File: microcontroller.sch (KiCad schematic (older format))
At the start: 22 parts, among them J7 I2C, SW1 SW_Push, U2 LM1117-5.0, U3 Teensy3.2

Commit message: Add ESP-32S symbol and footprint, start integration
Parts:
- removed C6, C7: 100nF tantal, Capacitor_SMD:C_0805_2012Metric_Pad1.15x1.40mm_HandSolder, symbol Device:C
- removed D7: 1N5817, Diode_SMD:D_SMA, symbol Device:D
- removed U2: LM1117-5.0, Package_TO_SOT_SMD:SOT-223-3_TabPin2, symbol Regulator_Linear:LM1117-5.0
- added U?: ESP32-DEVKITC-32D, MODULE_ESP32-DEVKITC-32D, symbol ESP32-DEVKITC-32D:ESP32-DEVKITC-32D
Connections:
- net labels removed: VUSB
- wire segments 69 -> 55
- no-connect marks 32 -> 45
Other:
- note added: "5...15 V DC"
- note added: "Bidirectional\nBreakdown Voltage: 15.2-16.8 V"
- note added: "Default I2C: SDA: GPIO 21, SCL: GPIO 22"
- note added: "ESP32 Pin Info:\nGPIO 6-11: Do not use! (onboard SPI Flash)\nGPIO 34,35: Input only\n"
- note added: "Ioutmax=1 A (AMS1117-3.3)"
- note added: "Serial0 (USB)"
- note added: "Serial2 (WT32i)"
- note added: "Vin=4.3...15 V"
- note added: "external 5k pullup"
- note added: "onboard LED"
- note removed: "6...20 V DC"
- note removed: "Ioutmax=250 mA"
- note removed: "Serial3"
- note removed: "This Diode should be solderd to protect the USB\nport when external voltage is present. To make it \nwork, a trace on the teensy must be cut."
- moved on the sheet: D6, U3

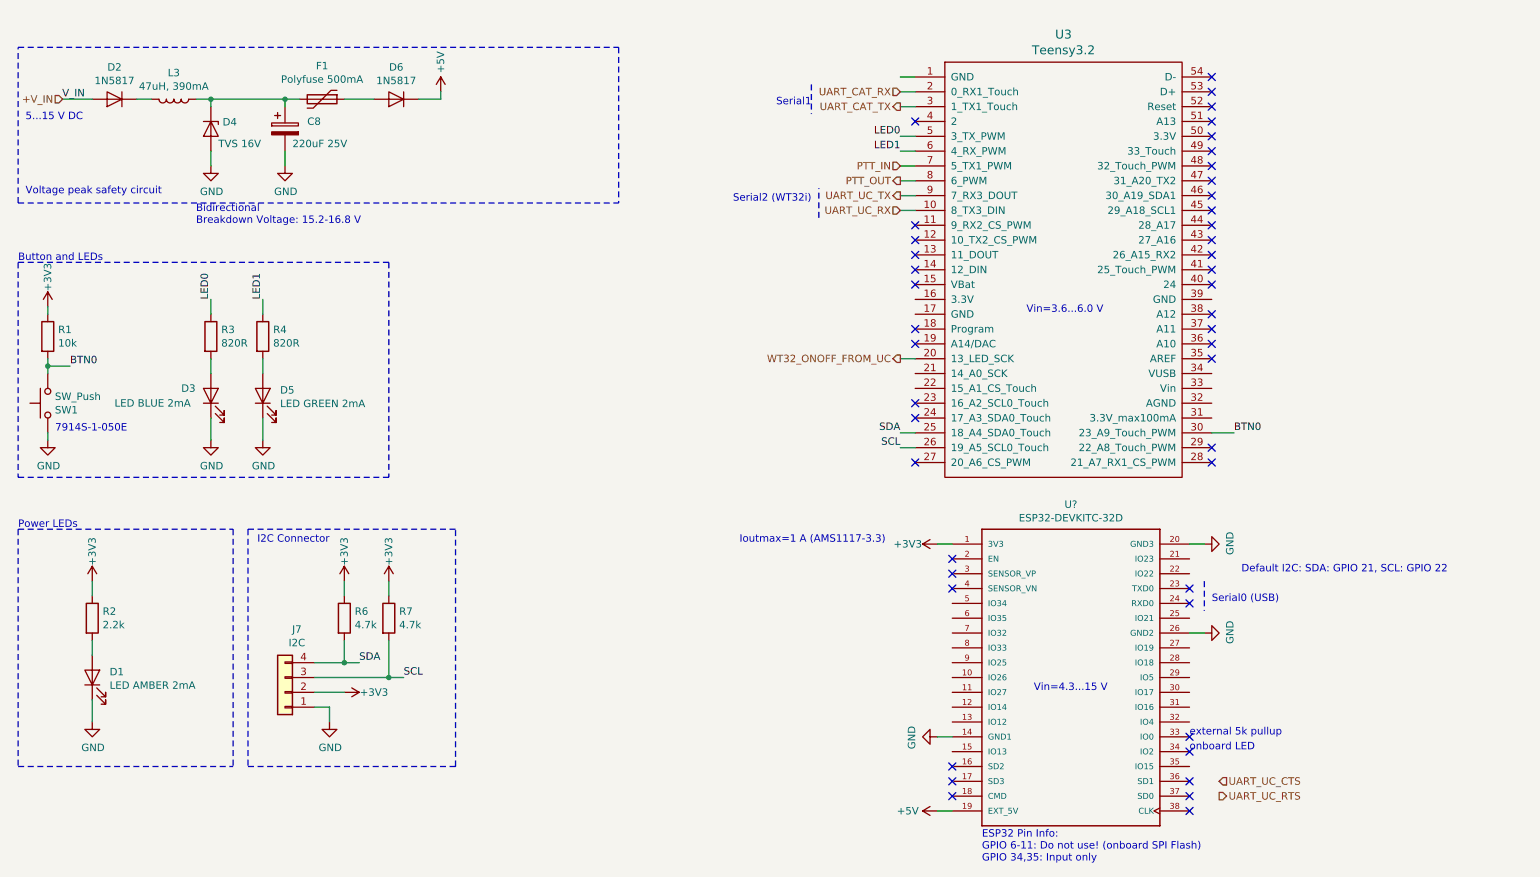
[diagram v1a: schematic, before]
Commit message: Assigned Pins to ESP32 and removed Teensy [#1]
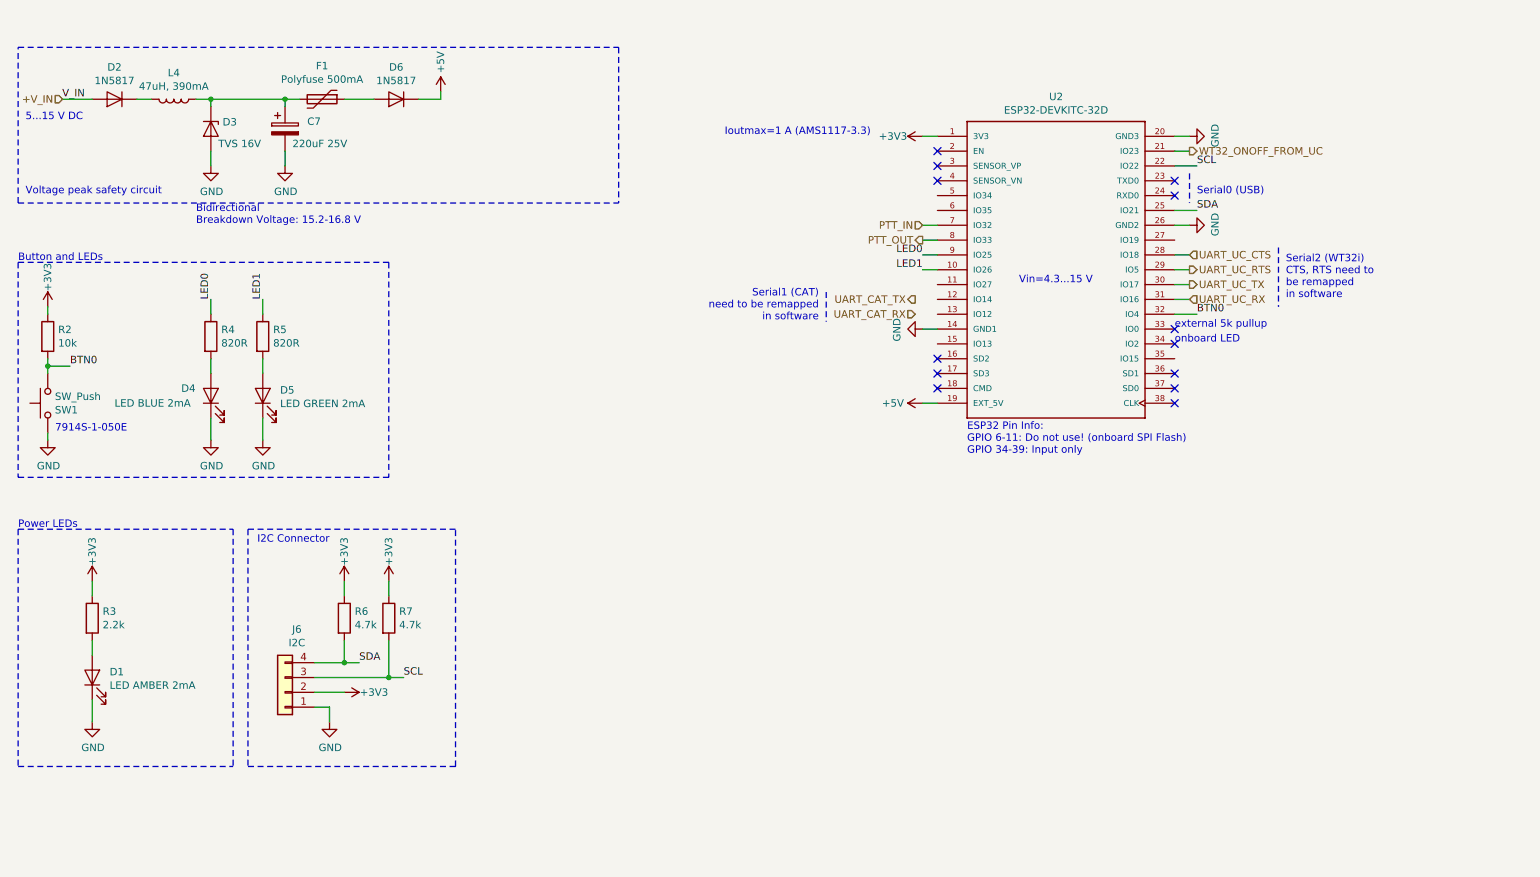
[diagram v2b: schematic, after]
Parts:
- removed U3: Teensy3.2, teensy:Teensy30_31_32_LC_stripped, symbol teensy:Teensy3.2
- U2: renamed from U?; footprint MODULE_ESP32-DEVKITC-32D -> ESP32-DEVKITC-32D:MODULE_ESP32-DEVKITC-32D
- renumbered C8 to C7, D4 to D3, D3 to D4, J7 to J6, L3 to L4, R1 to R2, R2 to R3, R3 to R4, R4 to R5
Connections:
- net BTN0: now also U2.32 (IO4)
- net LED0: now also U2.9 (IO25)
- net LED1: now also U2.10 (IO26)
- net PTT_IN: now also U2.7 (IO32)
- net PTT_OUT: now also U2.8 (IO33)
- net SCL: now also U2.22 (IO22)
- net SDA: now also U2.25 (IO21)
- net UART_UC_CTS: now also U2.28 (IO18)
- net UART_UC_RTS: now also U2.29 (IO5)
- net UART_UC_RX: now also U2.31 (IO16)
- net UART_UC_TX: now also U2.30 (IO17)
- net WT32_ONOFF_FROM_UC: now also U2.21 (IO23)
- no-connect marks 45 -> 13
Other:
- note added: "ESP32 Pin Info:\nGPIO 6-11: Do not use! (onboard SPI Flash)\nGPIO 34-39: Input only\n"
- note added: "Serial1 (CAT)\nneed to be remapped \nin software"
- note added: "Serial2 (WT32i)\nCTS, RTS need to\nbe remapped \nin software"
- note removed: "Default I2C: SDA: GPIO 21, SCL: GPIO 22"
- note removed: "ESP32 Pin Info:\nGPIO 6-11: Do not use! (onboard SPI Flash)\nGPIO 34,35: Input only\n"
- note removed: "Serial1"
- note removed: "Serial2 (WT32i)"
- note removed: "Vin=3.6...6.0 V"
- moved on the sheet: U2

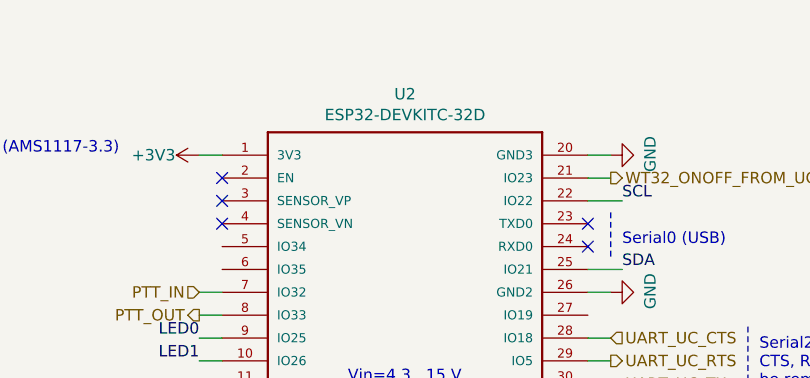
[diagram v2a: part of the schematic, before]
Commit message: Continued v4 [#1]
*removed all v3 stuff
* Resized board to max case size
* First deratsnesting
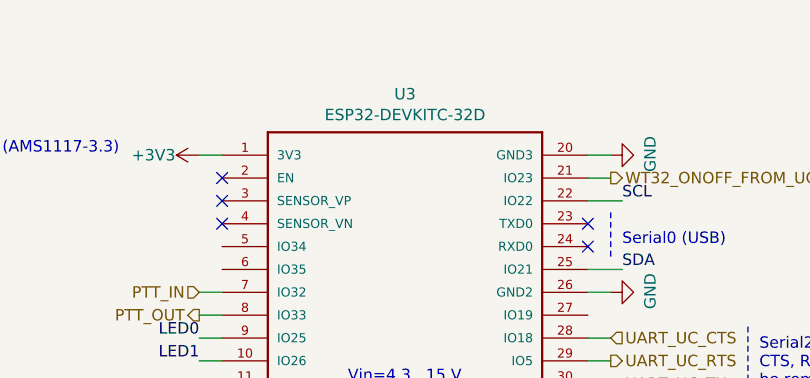
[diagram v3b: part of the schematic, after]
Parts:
- renumbered U2 to U3
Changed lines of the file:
@@
 Connection ~ 2500 1050
 $Comp
-L ESP32-DEVKITC-32D:ESP32-DEVKITC-32D U2
+L ESP32-DEVKITC-32D:ESP32-DEVKITC-32D U3
 U 1 1 5D1E8FF9
 P 7700 2200
-F 0 "U2" H 7700 3367 50  0000 C CNN
+F 0 "U3" H 7700 3367 50  0000 C CNN
 F 1 "ESP32-DEVKITC-32D" H 7700 3276 50  0000 C CNN
 F 2 "ESP32-DEVKITC-32D:MODULE_ESP32-DEVKITC-32D" H 7700 2200 50  0001 L BNN

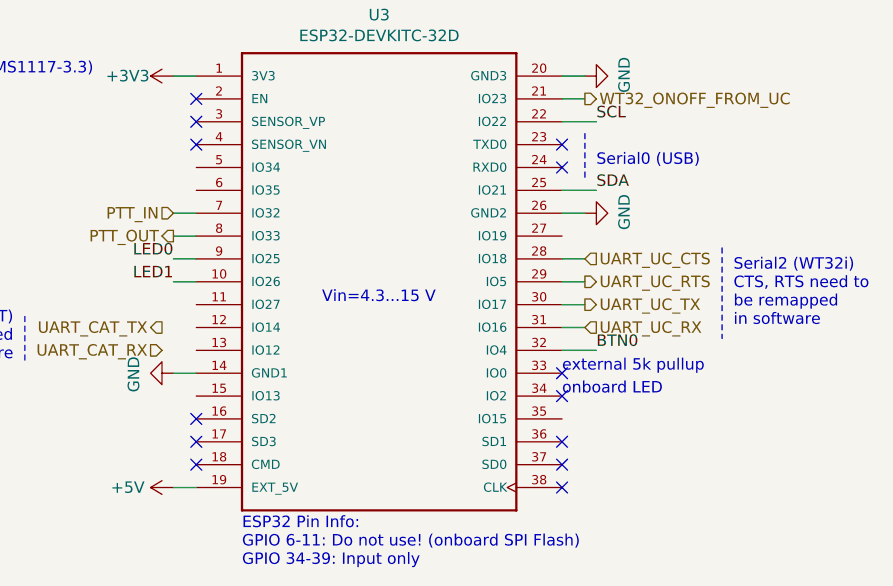
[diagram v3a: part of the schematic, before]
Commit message: [#1] Refined Schematic
* Removed RTS CTS
* Added 15pF capacitator to audio IN+
* Removed PTT jumper
* Added pull-up jumper
* Added solder jmpr bypass to RV
* Changed button footprint to SMD version
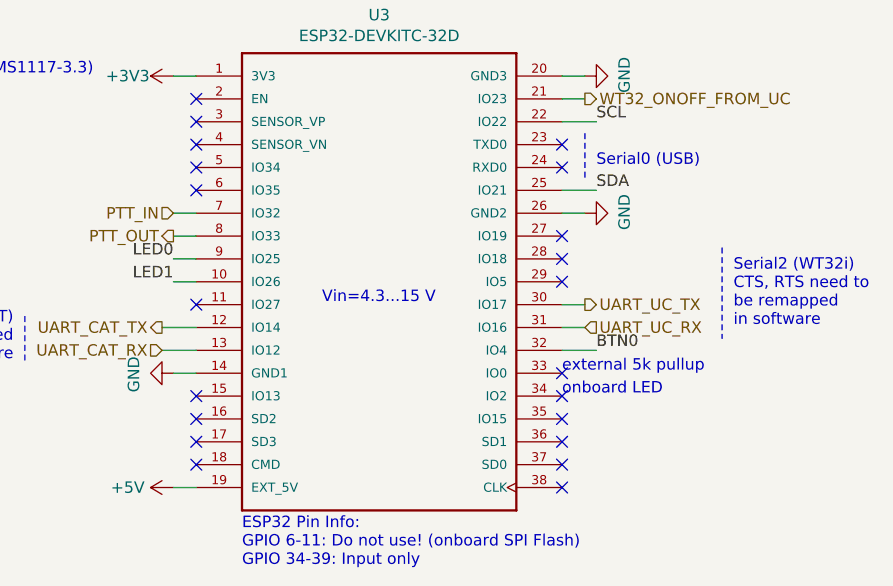
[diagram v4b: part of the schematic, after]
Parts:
- L4: Notes (none) -> to be verified
- SW1: footprint Button_Switch_THT:SW_Tactile_SKHH_Angled -> Button_Switch_SMD:Panasonic_EVQPUL_EVQPUC; Mouser Best.Nr. 611-PTS645VK832 -> 667-EVQ-PUL02K
- U3: Mouser Best.Nr. (none) -> TBD
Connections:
- net UART_CAT_RX: now also U3.13 (IO12)
- net UART_CAT_TX: now also U3.12 (IO14)
- net UART_UC_CTS: no longer names the net of U3.28 (IO18)
- net UART_UC_RTS: no longer names the net of U3.29 (IO5)
- no-connect marks 13 -> 21
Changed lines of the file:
@@
 EESchema Schematic File Version 4
 LIBS:bt-trx-dev-board-cache
-EELAYER 26 0
+EELAYER 29 0
 EELAYER END
 $Descr A4 11693 8268
@@
 F 0 "SW1" V 946 3052 50  0000 R CNN
 F 1 "SW_Push" V 855 3052 50  0000 R CNN
-F 2 "Button_Switch_THT:SW_Tactile_SKHH_Angled" H 900 3300 50  0001 C CNN
+F 2 "Button_Switch_SMD:Panasonic_EVQPUL_EVQPUC" H 900 3300 50  0001 C CNN
 F 3 "" H 900 3300 50  0001 C CNN
-F 4 "" H -2750 -2500 50  0001 C CNN "Reichelt Best.Nr."
-F 5 " 611-PTS645VK832" H -2750 -2500 50  0001 C CNN "Mouser Best.Nr."
+F 4 " 667-EVQ-PUL02K" H -2750 -2500 50  0001 C CNN "Mouser Best.Nr."
 	1    900  3100
 	0    -1   1    0
@@
 F 2 "Resistor_SMD:R_0805_2012Metric_Pad1.15x1.40mm_HandSolder" V 830 2650 50  0001 C CNN
 F 3 "~" H 900 2650 50  0001 C CNN
-F 4 "" H -2750 -2500 50  0001 C CNN "Reichelt Best.Nr."
-F 5 "603-RC0805FR-0710KL" H -2750 -2500 50  0001 C CNN "Mouser Best.Nr."
+F 4 "603-RC0805FR-0710KL" H -2750 -2500 50  0001 C CNN "Mouser Best.Nr."
 	1    900  2650
 	1    0    0    -1
@@
 F 2 "Resistor_SMD:R_0805_2012Metric_Pad1.15x1.40mm_HandSolder" V 1930 2650 50  0001 C CNN
 F 3 "~" H 2000 2650 50  0001 C CNN
-F 4 "" H -2750 -2500 50  0001 C CNN "Reichelt Best.Nr."
-F 5 "603-RC0805JR-07820RL" H -2750 -2500 50  0001 C CNN "Mouser Best.Nr."
+F 4 "603-RC0805JR-07820RL" H -2750 -2500 50  0001 C CNN "Mouser Best.Nr."
 	1    2000 2650
 	1    0    0    -1
@@
 F 2 "Kingbright:APA2107LSECK" H 2000 3050 50  0001 C CNN
 F 3 "~" H 2000 3050 50  0001 C CNN
-F 4 "" H -2750 -2500 50  0001 C CNN "Reichelt Best.Nr."
-F 5 "604-APA2107LVBCD" H -2750 -2500 50  0001 C CNN "Mouser Best.Nr."
+F 4 "604-APA2107LVBCD" H -2750 -2500 50  0001 C CNN "Mouser Best.Nr."
 	1    2000 3050
 	0    -1   -1   0
@@
 F 2 "Resistor_SMD:R_0805_2012Metric_Pad1.15x1.40mm_HandSolder" V 2280 2650 50  0001 C CNN
 F 3 "~" H 2350 2650 50  0001 C CNN
-F 4 "" H -2750 -2500 50  0001 C CNN "Reichelt Best.Nr."
-F 5 "603-RC0805JR-07820RL" H -2750 -2500 50  0001 C CNN "Mouser Best.Nr."
+F 4 "603-RC0805JR-07820RL" H -2750 -2500 50  0001 C CNN "Mouser Best.Nr."
 	1    2350 2650
 	1    0    0    -1
@@
 F 2 "Kingbright:APA2107LSECK" H 2350 3050 50  0001 C CNN
 F 3 "~" H 2350 3050 50  0001 C CNN
-F 4 "" H -2750 -2500 50  0001 C CNN "Reichelt Best.Nr."
-F 5 "604-APA2107LZGCK" H -2750 -2500 50  0001 C CNN "Mouser Best.Nr."
+F 4 "604-APA2107LZGCK" H -2750 -2500 50  0001 C CNN "Mouser Best.Nr."
 	1    2350 3050
 	0    -1   -1   0
@@
 F 2 "Fuse:Fuse_1206_3216Metric_Pad1.42x1.75mm_HandSolder" H 2800 850 50  0001 L CNN
 F 3 "~" H 2750 1050 50  0001 C CNN
-F 4 "" H -2650 -50 50  0001 C CNN "Reichelt Best.Nr."
-F 5 "530-0ZCJ0025AF2E" H -2650 -50 50  0001 C CNN "Mouser Best.Nr."
+F 4 "530-0ZCJ0025AF2E" H -2650 -50 50  0001 C CNN "Mouser Best.Nr."
 	1    2750 1050
 	0    1    1    0
@@
 F 3 "~" H 1750 1050 50  0001 C CNN
 F 4 "710-74438335470" V 1750 1050 50  0001 C CNN "Mouser Best.Nr."
-F 5 "" V 1750 1050 50  0001 C CNN "Notes"
+F 5 "to be verified" V 1750 1050 50  0001 C CNN "Notes"
 	1    1750 1050
 	0    1    1    0
@@
 F 3 "~" H 2000 1250 50  0001 C CNN
 F 4 "652-P6SMB16CA" V 2000 1250 50  0001 C CNN "Mouser Best.Nr."
-F 5 "" V 2000 1250 50  0001 C CNN "Notes"
 	1    2000 1250
 	0    1    1    0
@@
 F 2 "Resistor_SMD:R_0805_2012Metric_Pad1.15x1.40mm_HandSolder" V 1130 4550 50  0001 C CNN
 F 3 "~" H 1200 4550 50  0001 C CNN
-F 4 "" H -7550 1050 50  0001 C CNN "Reichelt Best.Nr."
-F 5 "603-RC0805JR-072K2L " H -7550 1050 50  0001 C CNN "Mouser Best.Nr."
+F 4 "603-RC0805JR-072K2L " H -7550 1050 50  0001 C CNN "Mouser Best.Nr."
 	1    1200 4550
 	1    0    0    -1
@@
 F 2 "Kingbright:APA2107LSECK" H 1200 4950 50  0001 C CNN
 F 3 "~" H 1200 4950 50  0001 C CNN
-F 4 "" H -7550 1050 50  0001 C CNN "Reichelt Best.Nr."
-F 5 "604-APA2107LSECKJ4RV" H -7550 1050 50  0001 C CNN "Mouser Best.Nr."
+F 4 "604-APA2107LSECKJ4RV" H -7550 1050 50  0001 C CNN "Mouser Best.Nr."
 	1    1200 4950
 	0    -1   -1   0
@@
 Text HLabel 6800 1900 0    50   Input ~ 0
 PTT_IN
-Text HLabel 8600 2100 2    50   Input ~ 0
-UART_UC_CTS
 $Comp
 L power:+3V3 #PWR?
@@
 F 2 "Resistor_SMD:R_0805_2012Metric_Pad1.15x1.40mm_HandSolder" V 2830 4550 50  0001 C CNN
 F 3 "~" H 2900 4550 50  0001 C CNN
-F 4 "" H -750 -600 50  0001 C CNN "Reichelt Best.Nr."
-F 5 "603-RC0805JR-074K7L" H -750 -600 50  0001 C CNN "Mouser Best.Nr."
+F 4 "603-RC0805JR-074K7L" H -750 -600 50  0001 C CNN "Mouser Best.Nr."
 	1    2900 4550
 	1    0    0    -1
@@
 F 2 "Resistor_SMD:R_0805_2012Metric_Pad1.15x1.40mm_HandSolder" V 3130 4550 50  0001 C CNN
 F 3 "~" H 3200 4550 50  0001 C CNN
-F 4 "" H -450 -600 50  0001 C CNN "Reichelt Best.Nr."
-F 5 "603-RC0805JR-074K7L" H -450 -600 50  0001 C CNN "Mouser Best.Nr."
+F 4 "603-RC0805JR-074K7L" H -450 -600 50  0001 C CNN "Mouser Best.Nr."
 	1    3200 4550
 	1    0    0    -1
@@
 F 7 "ESP32-DEVKITC-32D" H 7700 2200 50  0001 L BNN "Field7"
 F 8 "None" H 7700 2200 50  0001 L BNN "Field8"
+F 9 "TBD" H 7700 2200 50  0001 C CNN "Mouser Best.Nr."
 	1    7700 2200
 	1    0    0    -1
@@
 Wire Notes Line
 	8600 1550 8600 1750
-Text HLabel 8600 2200 2    50   Output ~ 0
-UART_UC_RTS
 Text Notes 7450 2300 0    50   ~ 0
 Vin=4.3...15 V
@@
 	9200 2050 9200 2450
 Wire Wire Line
-	8500 2100 8600 2100
-Wire Wire Line
-	8500 2200 8600 2200
-Wire Wire Line
 	8500 2300 8600 2300
 Wire Wire Line
@@
 Text Notes 6100 2550 2    50   ~ 0
 Serial1 (CAT)\nneed to be remapped \nin software
+Wire Wire Line
+	6750 2400 6900 2400
+Wire Wire Line
+	6900 2500 6750 2500
+NoConn ~ 8500 2000
+NoConn ~ 8500 2800
+NoConn ~ 6900 1700
+NoConn ~ 6900 1800
+NoConn ~ 6900 2700
+NoConn ~ 6900 2300
+NoConn ~ 8500 2100
+NoConn ~ 8500 2200
 $EndSCHEMATC

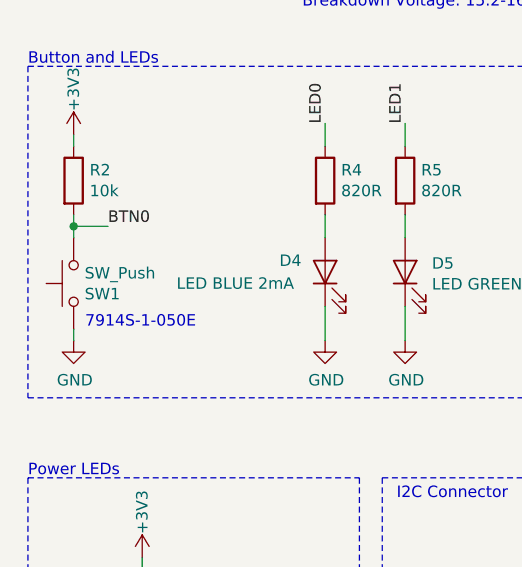
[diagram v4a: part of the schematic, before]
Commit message: [#1] Reworked audio path
* Swaped LN and LP for better reading
* Rearanged audio-in cirquid
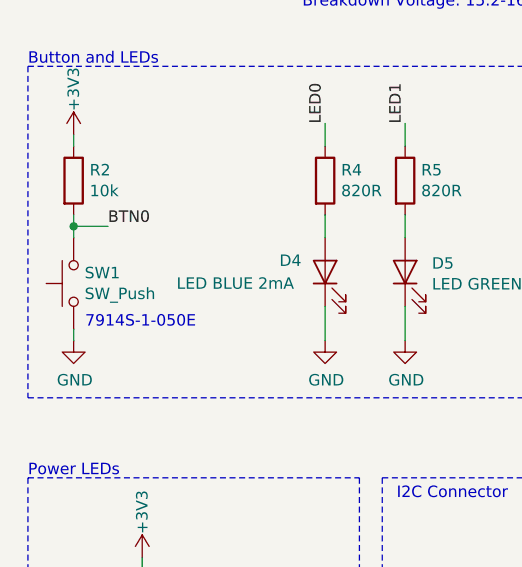
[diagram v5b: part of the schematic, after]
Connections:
- net BTN0: now also SW1.2; no longer SW1.1
- net GND: now also SW1.1; no longer SW1.2
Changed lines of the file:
@@
 F 4 " 667-EVQ-PUL02K" H -2750 -2500 50  0001 C CNN "Mouser Best.Nr."
 	1    900  3100
-	0    -1   1    0
+	0    -1   -1   0
 $EndComp
 $Comp
